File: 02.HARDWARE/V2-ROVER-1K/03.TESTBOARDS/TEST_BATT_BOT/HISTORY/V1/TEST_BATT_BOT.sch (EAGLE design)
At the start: 6 parts

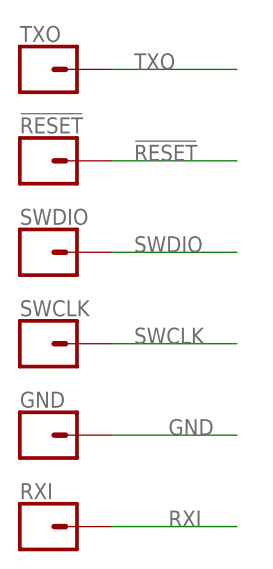
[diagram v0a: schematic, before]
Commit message: Pedido PCBWAY compatible con v2 de PCB CONN
PCB CONN ha movido los testpoints y se añade RXI
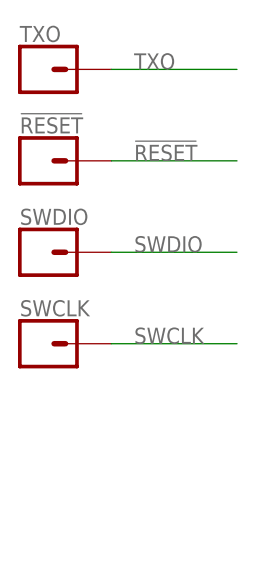
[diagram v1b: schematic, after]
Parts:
- removed GND, RXI: (no value), SparkFun-Connectors:CONN_01POGOPIN_HOLE_LARGE
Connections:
- removed net GND: GND.1
- removed net RXI: RXI.1
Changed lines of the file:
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@@
 <drawing>
 <settings>
-<setting alwaysvectorfont="no"/>
+<setting alwaysvectorfont="yes"/>
 <setting verticaltext="up"/>
 </settings>
-<grid distance="0.1" unitdist="inch" unit="inch" style="lines" multiple="1" display="no" altdistance="0.01" altunitdist="inch" altunit="inch"/>
+<grid distance="0.1" unitdist="inch" unit="inch" style="lines" multiple="1" display="yes" altdistance="0.01" altunitdist="inch" altunit="inch"/>
 <layers>
 <layer number="1" name="Top" color="4" fill="1" visible="no" active="no"/>
@@
 <part name="SWDIO" library="SparkFun-Connectors" deviceset="CONN_01" device="POGOPIN_HOLE_LARGE"/>
 <part name="TXO" library="SparkFun-Connectors" deviceset="CONN_01" device="POGOPIN_HOLE_LARGE"/>
-<part name="GND" library="SparkFun-Connectors" deviceset="CONN_01" device="POGOPIN_HOLE_LARGE"/>
-<part name="RXI" library="SparkFun-Connectors" deviceset="CONN_01" device="POGOPIN_HOLE_LARGE"/>
 </parts>
 <sheets>
@@
 <attribute name="NAME" x="69.85" y="89.408" size="1.778" layer="95" font="vector"/>
 </instance>
-<instance part="GND" gate="G$1" x="72.39" y="45.72" smashed="yes">
-<attribute name="VALUE" x="69.85" y="40.894" size="1.778" layer="96" font="vector"/>
-<attribute name="NAME" x="69.85" y="48.768" size="1.778" layer="95" font="vector"/>
-</instance>
-<instance part="RXI" gate="G$1" x="72.39" y="35.56" smashed="yes">
-<attribute name="VALUE" x="69.85" y="30.734" size="1.778" layer="96" font="vector"/>
-<attribute name="NAME" x="69.85" y="38.608" size="1.778" layer="95" font="vector"/>
-</instance>
 </instances>
 <busses>
@@
 </segment>
 </net>
-<net name="GND" class="0">
-<segment>
-<pinref part="GND" gate="G$1" pin="1"/>
-<wire x1="80.01" y1="45.72" x2="93.98" y2="45.72" width="0.1524" layer="91"/>
-<label x="86.36" y="45.72" size="1.778" layer="95"/>
-</segment>
-</net>
-<net name="RXI" class="0">
-<segment>
-<pinref part="RXI" gate="G$1" pin="1"/>
-<wire x1="80.01" y1="35.56" x2="93.98" y2="35.56" width="0.1524" layer="91"/>
-<label x="86.36" y="35.56" size="1.778" layer="95"/>
-</segment>
-</net>
